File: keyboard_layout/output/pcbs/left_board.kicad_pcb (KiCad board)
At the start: 2 copper layers, 144.1 x 115 mm, 66 parts

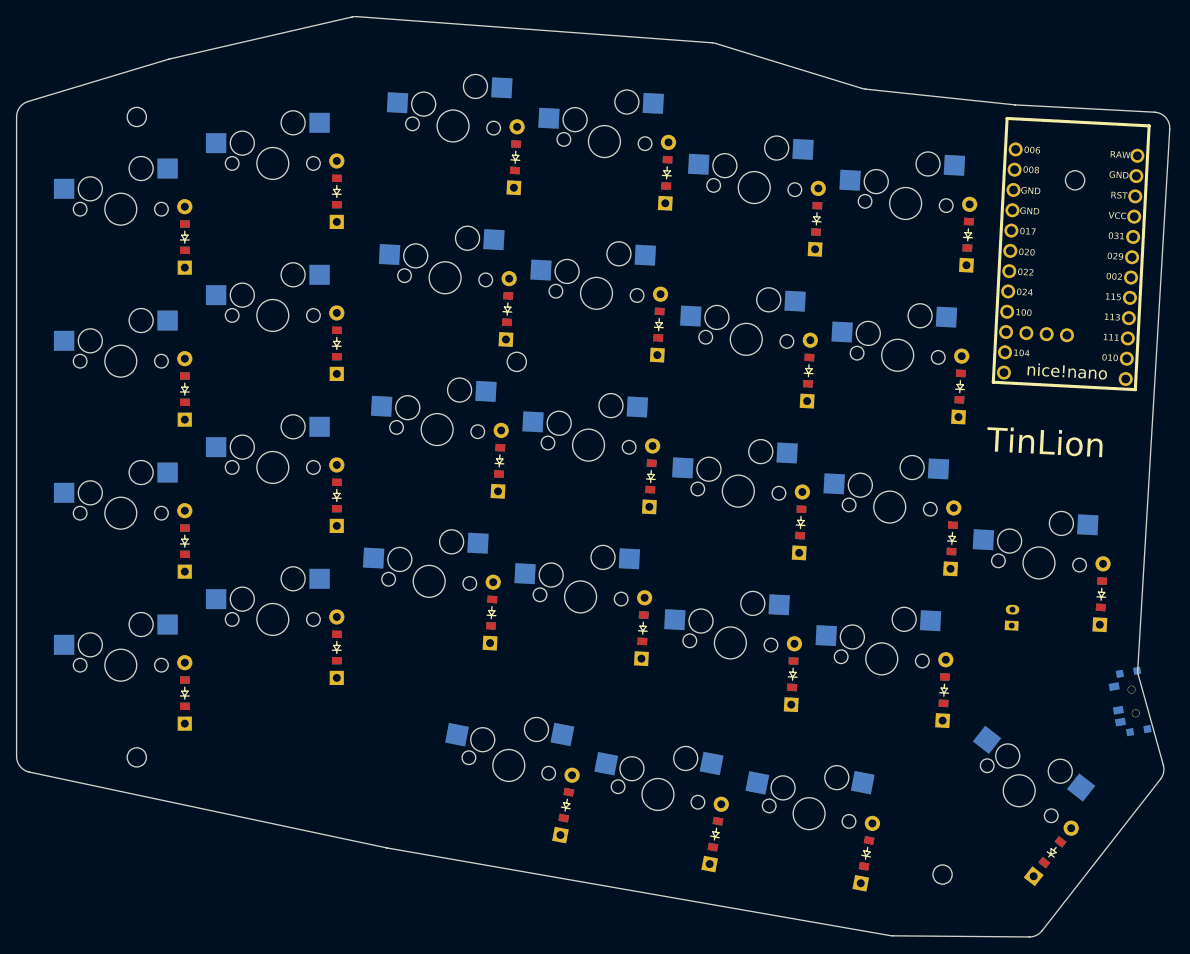
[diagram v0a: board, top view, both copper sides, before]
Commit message: Move mount screw holes
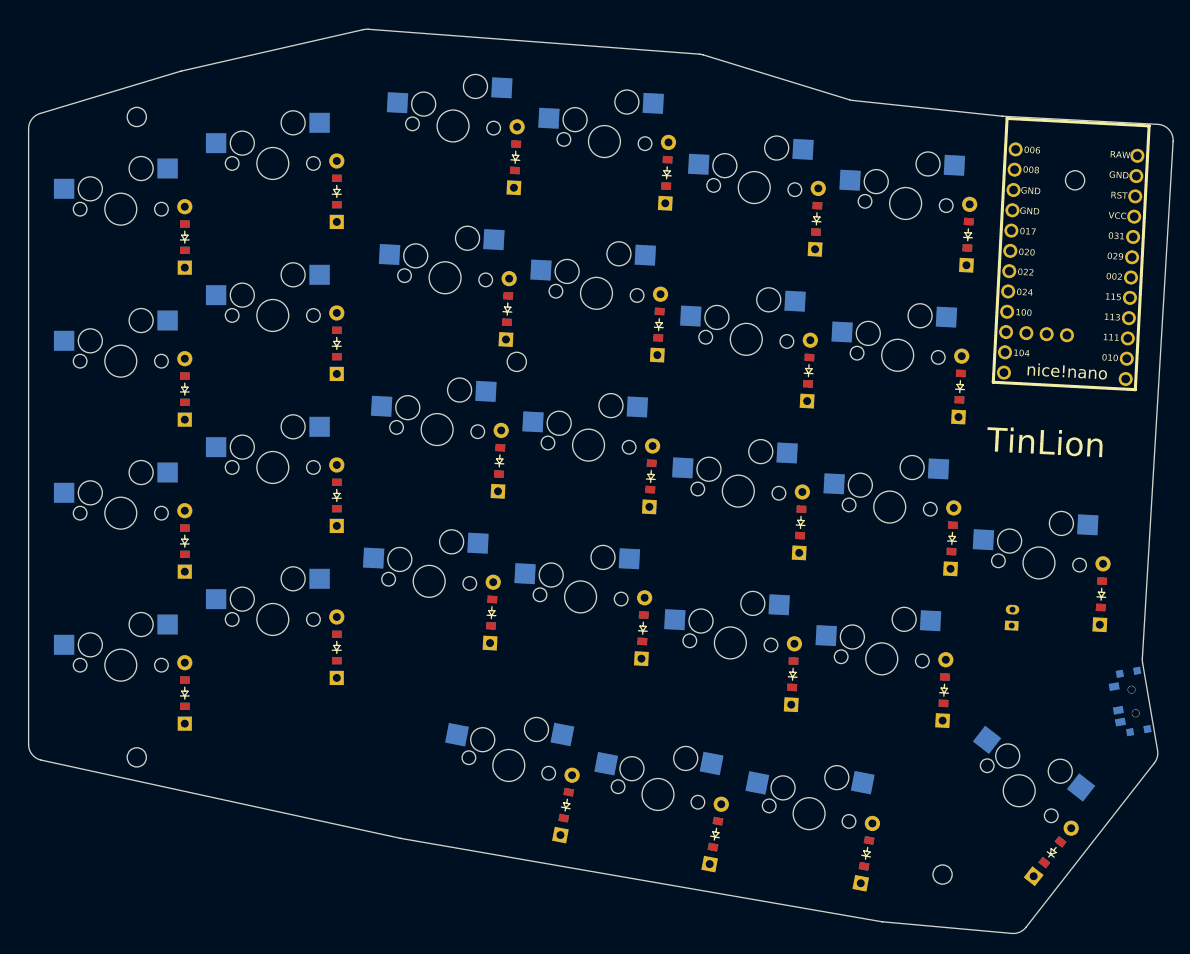
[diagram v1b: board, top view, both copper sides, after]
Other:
- board size 144.1 x 115 mm -> 143.1 x 113 mm
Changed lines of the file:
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@@
                 (effects (font (size 3 3) (thickness 0.4) ) (justify left))
             )
-  (gr_line (start -13.025 11.404784244100759) (end -13.025 -68.5380634051579) (angle 90) (layer Edge.Cuts) (width 0.15))
-(gr_line (start -11.60108277241664 -70.45329931345469) (end 5.911850316224387 -75.72100523985381) (angle 90) (layer Edge.Cuts) (width 0.15))
-(gr_line (start 6.039263710502721 -75.75479363658964) (end 28.91334846581312 -81.02045437331321) (angle 90) (layer Edge.Cuts) (width 0.15))
-(gr_line (start 29.508885244490674 -81.06603027560415) (end 73.92128997139757 -77.79583202507767) (angle 90) (layer Edge.Cuts) (width 0.15))
-(gr_line (start 74.36155953417676 -77.71310789830906) (end 92.685712164064 -72.08576305145405) (angle 90) (layer Edge.Cuts) (width 0.15))
-(gr_line (start 93.06334831696502 -72.00864203310623) (end 111.7401164745767 -70.0414200984346) (angle 90) (layer Edge.Cuts) (width 0.15))
-(gr_line (start 111.84494528004161 -70.03315810283766) (end 129.2298847487764 -69.1220519861765) (angle 90) (layer Edge.Cuts) (width 0.15))
-(gr_line (start 131.12171614382393 -67.00658049167669) (end 127.1199559180007 0.5796557503790609) (angle 90) (layer Edge.Cuts) (width 0.15))
-(gr_line (start 127.18956979936688 1.2336823833675794) (end 130.31708474844757 12.480817359715502) (angle 90) (layer Edge.Cuts) (width 0.15))
-(gr_line (start 129.9662167677175 14.247954544189525) (end 115.15621154005028 33.203896698935154) (angle 90) (layer Edge.Cuts) (width 0.15))
-(gr_line (start 113.56383160132178 33.97250684826114) (end 96.50373431280677 33.832963426109266) (angle 90) (layer Edge.Cuts) (width 0.15))
-(gr_line (start 96.17685491363135 33.803357125298064) (end 33.26338233504851 22.843612454957245) (angle 90) (layer Edge.Cuts) (width 0.15))
-(gr_line (start 33.191561910440576 22.829743370951512) (end -11.44005822460793 13.361241960095024) (angle 90) (layer Edge.Cuts) (width 0.15))
-(gr_arc (start -11.025 -68.5380634051579) (end -11.6010828 -70.4532993051579) (angle -73.25926693492322) (layer Edge.Cuts) (width 0.15))
-(gr_arc (start 6.48793308864103 -73.80576933155703) (end 6.03926368864103 -75.75479363155704) (angle -3.7769744047999154) (layer Edge.Cuts) (width 0.15))
-(gr_arc (start 29.362017843951428 -79.0714300682806) (end 29.50888524395143 -81.0660302682806) (angle -17.174990398254295) (layer Edge.Cuts) (width 0.15))
-(gr_arc (start 73.77442257085832 -75.80123181775414) (end 74.36155957085832 -77.71310791775414) (angle -12.860485452222477) (layer Edge.Cuts) (width 0.15))
-(gr_arc (start 93.27284912738244 -73.99763913200896) (end 92.68571212738244 -72.08576303200896) (angle -11.058930695449448) (layer Edge.Cuts) (width 0.15))
-(gr_arc (start 111.94961728499412 -72.03041719733733) (end 111.74011648499412 -70.04142009733732) (angle -3.01278388687615) (layer Edge.Cuts) (width 0.15))
-(gr_arc (start 129.1252127438239 -67.12479289167683) (end 131.1217161438239 -67.00658049167683) (angle -90.38850813719492) (layer Edge.Cuts) (width 0.15))
-(gr_arc (start 129.11645931800072 0.6978681503787811) (end 127.11995591800073 0.5796557503787811) (angle -18.928276491823766) (layer Edge.Cuts) (width 0.15))
-(gr_arc (start 128.3901952298136 13.0166315927043) (end 129.9662167298136 14.2479544927043) (angle -53.539765224291) (layer Edge.Cuts) (width 0.15))
-(gr_arc (start 113.58019000214637 31.97257374744993) (end 113.56383160214637 33.97250684744993) (angle -52.46863941096757) (layer Edge.Cuts) (width 0.15))
-(gr_arc (start 96.52009271363134 31.833030325298065) (end 96.17685491363135 33.803357125298064) (angle -9.413319927295163) (layer Edge.Cuts) (width 0.15))
-(gr_arc (start 33.606620135048516 20.87328565495725) (end 33.19156193504852 22.82974335495725) (angle -2.0956320832466986) (layer Edge.Cuts) (width 0.15))
-(gr_arc (start -11.025 11.404784244100759) (end -13.025 11.404784244100759) (angle -78.02240910096583) (layer Edge.Cuts) (width 0.15))
+  (gr_line (start -11.525 9.913577784092134) (end -11.525 -67.03806340515791) (angle 90) (layer Edge.Cuts) (width 0.15))
+(gr_line (start -10.101082772416635 -68.95329931345468) (end 7.409572473708378 -74.2203200888023) (angle 90) (layer Edge.Cuts) (width 0.15))
+(gr_line (start 7.541618846125022 -74.2551691805055) (end 30.33349488631909 -79.44490304445853) (angle 90) (layer Edge.Cuts) (width 0.15))
+(gr_line (start 30.927405893791747 -79.48919454389697) (end 72.34638951795236 -76.37661611728166) (angle 90) (layer Edge.Cuts) (width 0.15))
+(gr_line (start 72.78365187379814 -76.29411569839812) (end 91.10926396406398 -70.66632265145405) (angle 90) (layer Edge.Cuts) (width 0.15))
+(gr_line (start 91.48690011696503 -70.58920163310623) (end 110.16366827392203 -68.62197969850354) (angle 90) (layer Edge.Cuts) (width 0.15))
+(gr_line (start 110.2684970793869 -68.6137177029066) (end 129.65008544136802 -67.59797165922595) (angle 90) (layer Edge.Cuts) (width 0.15))
+(gr_line (start 131.54188083641554 -65.48189456472619) (end 127.69172433813952 -0.7887567923867209) (angle 90) (layer Edge.Cuts) (width 0.15))
+(gr_line (start 127.71682273813957 -0.33273799238691026) (end 129.5961345840037 10.654237968498023) (angle 90) (layer Edge.Cuts) (width 0.15))
+(gr_line (start 129.2007871219076 12.222761719983339) (end 113.14635795684372 32.77149393312962) (angle 90) (layer Edge.Cuts) (width 0.15))
+(gr_line (start 111.39133861974085 33.53214477273045) (end 95.23446190169574 32.08029612043122) (angle 90) (layer Edge.Cuts) (width 0.15))
+(gr_line (start 95.07211090089473 32.05897732934519) (end 35.02822914254588 21.65842222274783) (angle 90) (layer Edge.Cuts) (width 0.15))
+(gr_line (start 34.944116138020455 21.641988843534005) (end -9.950461804525446 11.867799404878303) (angle 90) (layer Edge.Cuts) (width 0.15))
+(gr_arc (start -9.525 -67.03806340515791) (end -10.1010828 -68.95329930515791) (angle -73.25926693492313) (layer Edge.Cuts) (width 0.15))
+(gr_arc (start 7.98565524612502 -72.3050841805055) (end 7.54161884612502 -74.2551691805055) (angle -3.913133492551367) (layer Edge.Cuts) (width 0.15))
+(gr_arc (start 30.777531286319093 -77.49481804445853) (end 30.927405886319093 -79.48919454445853) (angle -17.12521949795436) (layer Edge.Cuts) (width 0.15))
+(gr_arc (start 72.19651491047969 -74.3822396178432) (end 72.78365191047969 -76.2941157178432) (angle -12.774097264770717) (layer Edge.Cuts) (width 0.15))
+(gr_arc (start 91.69640092738244 -72.57819873200896) (end 91.10926392738244 -70.66632263200896) (angle -11.058930695450243) (layer Edge.Cuts) (width 0.15))
+(gr_arc (start 110.37316908433944 -70.61097679740627) (end 110.16366828433944 -68.62197969740626) (angle -3.0127838868748995) (layer Edge.Cuts) (width 0.15))
+(gr_arc (start 129.54541343641552 -65.6007125647263) (end 131.5418809364155 -65.48189456472629) (angle -90.40588792604855) (layer Edge.Cuts) (width 0.15))
+(gr_arc (start 129.68819173813955 -0.6699387923868017) (end 127.69172423813956 -0.7887567923868016) (angle -13.112343718403451) (layer Edge.Cuts) (width 0.15))
+(gr_arc (start 127.62476558400371 10.991438768498142) (end 129.2007870840037 12.222761668498142) (angle -47.706452662016915) (layer Edge.Cuts) (width 0.15))
+(gr_arc (start 111.57033641893983 31.540170981644394) (end 111.39133861893983 33.53214478164439) (angle -57.13478046985142) (layer Edge.Cuts) (width 0.15))
+(gr_arc (start 95.41345970089472 30.08832232934519) (end 95.07211090089471 32.05897732934519) (angle -4.692252290154443) (layer Edge.Cuts) (width 0.15))
+(gr_arc (start 35.369577942545895 19.687767222747834) (end 34.944116142545894 21.641988822747834) (angle -2.455406217633822) (layer Edge.Cuts) (width 0.15))
+(gr_arc (start -9.525 9.913577784092134) (end -11.525 9.913577784092134) (angle -77.71756154483364) (layer Edge.Cuts) (width 0.15))
 )

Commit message: gerberfiles added, leftright pcbs
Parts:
- removed the ? at (102.7, 26.2)
- removed the ? at (2.00, 11.5)
- removed the ? at (2.00, -68.5)
- removed the ? at (119.3, -60.6)
- removed the ? at (49.5, -37.9)
- added ?: , HOLE_M2_TH, F.Cu at (107.2, 123.7)
- added ?: , HOLE_M2_TH, F.Cu at (160.4, 187.8)
- added ?: , HOLE_M2_TH, F.Cu at (177.0, 101.0)
- added ?: , HOLE_M2_TH, F.Cu at (59.7, 93.1)
- added ?: , HOLE_M2_TH, F.Cu at (59.7, 173.1)
- moved S25 171.6 mm to (106.2, 174.1)
- moved S22 171.6 mm to (153.8, 141.8)
- moved D11 171.6 mm to (106.0, 117.1)
- moved D14 171.6 mm to (124.0, 138.0)
- moved S28 171.6 mm to (170.0, 177.3)
- moved D27 171.6 mm to (150.9, 185.1)
- moved D25 171.6 mm to (113.4, 179.1)
- moved S19 171.6 mm to (135.9, 120.9)
- moved S21 171.6 mm to (152.8, 160.8)
- moved D22 171.6 mm to (161.6, 145.7)
- moved D26 171.6 mm to (132.0, 182.7)
- moved D10 171.6 mm to (105.0, 136.1)
- moved D13 171.6 mm to (123.0, 157.0)
- moved D19 171.6 mm to (143.7, 124.8)
- moved S11 171.6 mm to (98.2, 113.2)
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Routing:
- net P031: track 0.00 -> 189.9 mm
- net P006: track 0.00 -> 188.9 mm
- net P113: track 0.00 -> 185.2 mm
- net P111: track 0.00 -> 185.2 mm
- net P029: track 0.00 -> 166.3 mm
- net P115: track 0.00 -> 152.2 mm
- net P002: track 0.00 -> 146.8 mm
- net P010: track 0.00 -> 145.8 mm
- net P008: track 0.00 -> 144.5 mm
- net P017: track 0.00 -> 128.1 mm
- net P020: track 0.00 -> 112.3 mm
- net GND: track 0.00 -> 78.7 mm
- net RAW: track 0.00 -> 71.7 mm
- net P104: track 0.00 -> 50.2 mm
- net pos: track 0.00 -> 14.9 mm
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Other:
- net class Default removed

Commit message: Update final keyboard pcb
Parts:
- removed the ? at (107.2, 123.7)
- removed the ? at (160.4, 187.8)
- removed the ? at (177.0, 101.0)
- removed the ? at (59.7, 93.1)
- removed the ? at (59.7, 173.1)
- added ?: , HOLE_M2_TH, F.Cu at (102.7, 26.2)
- added ?: , HOLE_M2_TH, F.Cu at (2.00, 9.53)
- added ?: , HOLE_M2_TH, F.Cu at (7.00, -68.5)
- added ?: , HOLE_M2_TH, F.Cu at (98.6, -66.7)
- added ?: , HOLE_M2_TH, F.Cu at (77.7, -31.0)
- added ?: , HOLE_M2_TH, F.Cu at (30.4, -37.4)
- moved S25 171.6 mm to (48.5, 12.5)
- moved S22 171.6 mm to (96.1, -19.8)
- moved D11 171.6 mm to (48.3, -44.5)
- moved D14 171.6 mm to (66.3, -23.6)
- moved S28 171.6 mm to (112.3, 15.7)
- moved D27 171.6 mm to (93.2, 23.5)
- moved D25 171.6 mm to (55.7, 17.5)
- moved S19 171.6 mm to (78.2, -40.7)
- moved S21 171.6 mm to (95.1, -0.79)
- moved D22 171.6 mm to (103.9, -15.8)
- moved D26 171.6 mm to (74.3, 21.1)
- moved D10 171.6 mm to (47.4, -25.5)
- moved D13 171.6 mm to (65.3, -4.62)
- moved D19 171.6 mm to (86.0, -36.8)
- moved S11 171.6 mm to (40.5, -48.4)
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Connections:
- D1 pad 1: P111 -> P115
- D10 pad 1: P113 -> P002
- D11 pad 1: P115 -> P029
- D12 pad 1: P002 -> P031
- D13 pad 1: P111 -> P115
- D14 pad 1: P113 -> P002
- D15 pad 1: P115 -> P029
- D16 pad 1: P002 -> P031
- D17 pad 1: P111 -> P115
- D18 pad 1: P113 -> P002
- D19 pad 1: P115 -> P029
- D2 pad 1: P113 -> P002
- D20 pad 1: P002 -> P031
- D21 pad 1: P111 -> P115
- D22 pad 1: P113 -> P002
- D23 pad 1: P115 -> P029
- D24 pad 1: P002 -> P031
- D25 pad 1: P010 -> P113
- D26 pad 1: P010 -> P113
- D27 pad 1: P010 -> P113
- D28 pad 1: P010 -> P113
- D29 pad 1: P113 -> P002
- D3 pad 1: P115 -> P029
- D4 pad 1: P002 -> P031
- D5 pad 1: P111 -> P115
- D6 pad 1: P113 -> P002
- D7 pad 1: P115 -> P029
- D8 pad 1: P002 -> P031
- D9 pad 1: P111 -> P115
- S1 pad 1: P006 -> P020
- S10 pad 1: P008 -> P024
- S11 pad 1: P008 -> P024
- S12 pad 1: P008 -> P024
- S13 pad 1: P029 -> P100
- S14 pad 1: P029 -> P100
- S15 pad 1: P029 -> P100
- S16 pad 1: P029 -> P100
- S17 pad 1: P017 -> P011
- S18 pad 1: P017 -> P011
- S19 pad 1: P017 -> P011
- S2 pad 1: P006 -> P020
- S20 pad 1: P017 -> P011
- S21 pad 1: P020 -> P104
- S22 pad 1: P020 -> P104
- S23 pad 1: P020 -> P104
- S24 pad 1: P020 -> P104
- S25 pad 1: P029 -> P100
- S26 pad 1: P017 -> P011
- S27 pad 1: P020 -> P104
- S28 pad 1: P104 -> P017
- S29 pad 1: P104 -> P017
- S3 pad 1: P006 -> P020
- S4 pad 1: P006 -> P020
- S5 pad 1: P031 -> P022
- S6 pad 1: P031 -> P022
- S7 pad 1: P031 -> P022
- S8 pad 1: P031 -> P022
- S9 pad 1: P008 -> P024
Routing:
- net P031: track 189.9 -> 0.00 mm
- net P006: track 188.9 -> 0.00 mm
- net P113: track 185.2 -> 0.00 mm
- net P111: track 185.2 -> 0.00 mm
- net P029: track 166.3 -> 0.00 mm
- net P115: track 152.2 -> 0.00 mm
- net P002: track 146.8 -> 0.00 mm
- net P010: track 145.8 -> 0.00 mm
- net P008: track 144.5 -> 0.00 mm
- net P017: track 128.1 -> 0.00 mm
- net P020: track 112.3 -> 0.00 mm
- net GND: track 78.7 -> 0.00 mm
- net RAW: track 71.7 -> 0.00 mm
- net P104: track 50.2 -> 0.00 mm
- net pos: track 14.9 -> 0.00 mm
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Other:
- net class Default added: clearance 0.2, trace_width 0.25, via_dia 0.8, via_drill 0.4
- board text added: "TINLION"
- board text removed: "TinLion"
